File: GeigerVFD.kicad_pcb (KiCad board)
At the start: 2 copper layers, 32 parts, among them IC1 LM555, IC2 TLC555, J3 C-EUC0805, Q1 BD137, T2 2N4401, T3 STN0214, T4 2N4401, U2 ESP32-DEVKITC-32D, U3 MAX6934, U4 FV651G

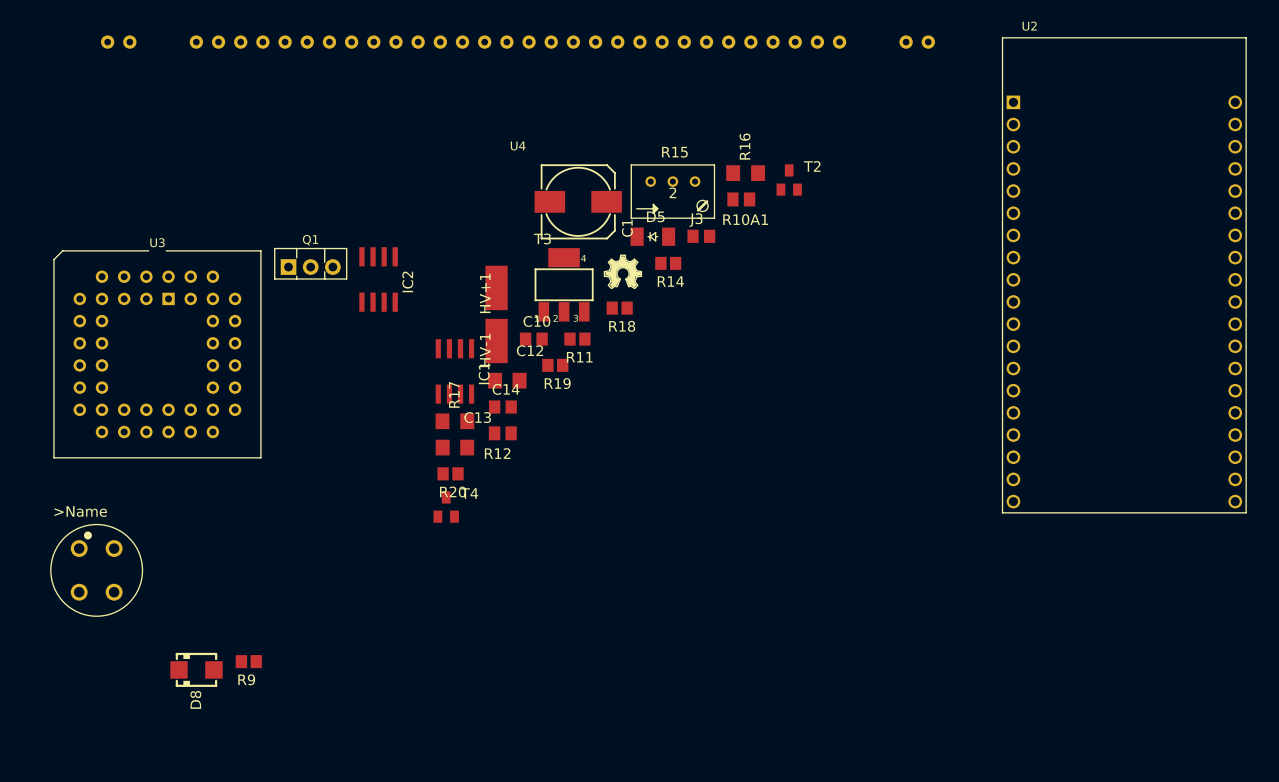
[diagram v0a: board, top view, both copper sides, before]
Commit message: Update footprints & fix bugs
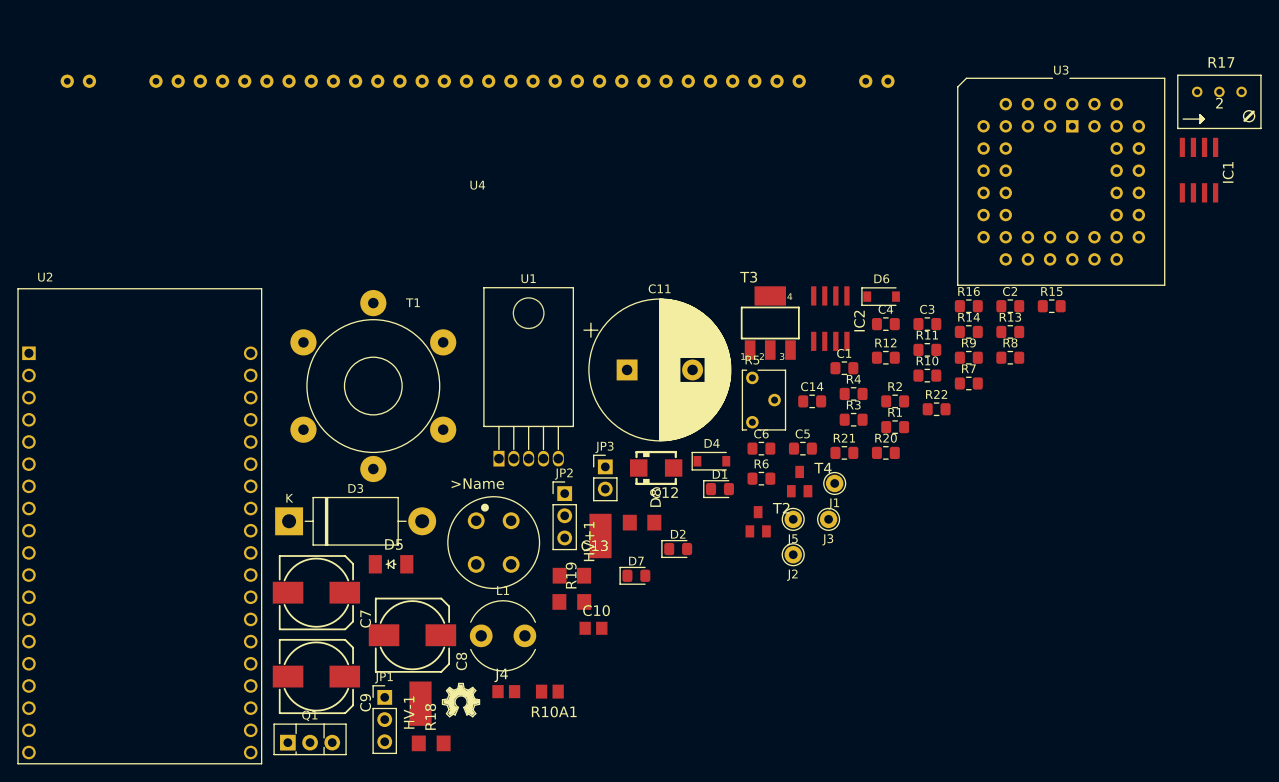
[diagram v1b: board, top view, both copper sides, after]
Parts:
- added C11: 1000µ, Capacitor_THT:CP_Radial_D16.0mm_P7.50mm, F.Cu at (519.9, 205.9)
- added C2: 10n, Capacitor_SMD:C_0805_2012Metric_Pad1.15x1.40mm_HandSolder, F.Cu at (563.8, 198.6)
- added C3: 100n, Capacitor_SMD:C_0805_2012Metric_Pad1.15x1.40mm_HandSolder, F.Cu at (554.3, 200.7)
- added C4: 330n, Capacitor_SMD:C_0805_2012Metric_Pad1.15x1.40mm_HandSolder, F.Cu at (549.6, 200.7)
- added C5: 100n, Capacitor_SMD:C_0805_2012Metric_Pad1.15x1.40mm_HandSolder, F.Cu at (540.1, 214.9)
- added C6: 100n, Capacitor_SMD:C_0805_2012Metric_Pad1.15x1.40mm_HandSolder, F.Cu at (535.3, 214.9)
- added C7: 10uF, PiGI-V1.1:153CLV-0810, F.Cu at (484.4, 231.4)
- added C8: 10uF, PiGI-V1.1:153CLV-0810, F.Cu at (495.4, 236.3)
- added C9: 220uF, PiGI-V1.1:153CLV-0810, F.Cu at (484.4, 241.0)
- added D1: green, LED_SMD:LED_0805_2012Metric_Pad1.15x1.40mm_HandSolder, F.Cu at (530.6, 219.6)
- added D2: yellow, LED_SMD:LED_0805_2012Metric_Pad1.15x1.40mm_HandSolder, F.Cu at (525.8, 226.4)
- added D3: 1N5822, Diode_THT:D_DO-201AD_P15.24mm_Horizontal, F.Cu at (481.2, 223.3)
- added D4: 1N4148, Diode_SMD:D_SOD-123, F.Cu at (529.6, 216.4)
- added D6: 1N4148, Diode_SMD:D_SOD-123, F.Cu at (549.1, 197.5)
- added D7: red, LED_SMD:LED_0805_2012Metric_Pad1.15x1.40mm_HandSolder, F.Cu at (521.0, 229.5)
- added J1: 5V, Connector_Pin:Pin_D1.0mm_L10.0mm, F.Cu at (543.7, 218.9)
- added J2: 3.3V, Connector_Pin:Pin_D1.0mm_L10.0mm, F.Cu at (539.0, 227.1)
- added J4: C-EUC0805, PiGI-V1.1:C0805, F.Cu at (506.1, 242.8)
- added J5: Pulse, Connector_Pin:Pin_D1.0mm_L10.0mm, F.Cu at (539.0, 223.1)
- added JP1: Jumper3, Connector_PinHeader_2.54mm:PinHeader_1x03_P2.54mm_Vertical, F.Cu at (492.2, 243.4)
- added JP2: Jumper3, Connector_PinHeader_2.54mm:PinHeader_1x03_P2.54mm_Vertical, F.Cu at (512.8, 220.1)
- added JP3: Jumper, Connector_PinHeader_2.54mm:PinHeader_1x02_P2.54mm_Vertical, F.Cu at (517.5, 217.0)
- added L1: 100µ, Inductor_THT:L_Radial_D7.8mm_P5.00mm_Fastron_07HCP, F.Cu at (503.2, 236.4)
- added R1: 1k, Resistor_SMD:R_0805_2012Metric_Pad1.15x1.40mm_HandSolder, F.Cu at (550.6, 212.5)
- added R10: 220k, Resistor_SMD:R_0805_2012Metric_Pad1.15x1.40mm_HandSolder, F.Cu at (554.3, 206.6)
- added R13: 1k, Resistor_SMD:R_0805_2012Metric_Pad1.15x1.40mm_HandSolder, F.Cu at (563.8, 201.6)
- added R2: 1k, Resistor_SMD:R_0805_2012Metric_Pad1.15x1.40mm_HandSolder, F.Cu at (550.6, 209.5)
- added R21: 100k, Resistor_SMD:R_0805_2012Metric_Pad1.15x1.40mm_HandSolder, F.Cu at (544.8, 215.4)
- added R22: 27k, Resistor_SMD:R_0805_2012Metric_Pad1.15x1.40mm_HandSolder, F.Cu at (555.4, 210.4)
- added R3: 2.2k, Resistor_SMD:R_0805_2012Metric_Pad1.15x1.40mm_HandSolder, F.Cu at (545.9, 211.6)
- added R4: 1k, Resistor_SMD:R_0805_2012Metric_Pad1.15x1.40mm_HandSolder, F.Cu at (545.9, 208.7)
- added R5: 100k, Potentiometer_THT:Potentiometer_Vishay_T73XX_Horizontal, F.Cu at (534.3, 206.8)
- added R6: 1k, Resistor_SMD:R_0805_2012Metric_Pad1.15x1.40mm_HandSolder, F.Cu at (535.3, 218.4)
- added R7: 2.2k, Resistor_SMD:R_0805_2012Metric_Pad1.15x1.40mm_HandSolder, F.Cu at (559.1, 207.5)
- added R8: 1k, Resistor_SMD:R_0805_2012Metric_Pad1.15x1.40mm_HandSolder, F.Cu at (563.8, 204.5)
- added T1: Transformer_1P_SS, Transformer_THT:Transformer_Toroid_Tapped_Horizontal_D14.0mm_Amidon-T50, F.Cu at (482.9, 212.8)
- added U1: LM2577, Package_TO_SOT_THT:TO-220-5_Horizontal_TabDown, F.Cu at (505.3, 216.1)
- C1: value 220uF -> 4.7n; footprint PiGI-V1.1:153CLV-0810 -> Capacitor_SMD:C_0805_2012Metric_Pad1.15x1.40mm_HandSolder
- C14: footprint PiGI-V1.1:C0805 -> Capacitor_SMD:C_0805_2012Metric_Pad1.15x1.40mm_HandSolder
- J3: value C-EUC0805 -> GND; footprint PiGI-V1.1:C0805 -> Connector_Pin:Pin_D1.0mm_L10.0mm
- R11: value 330 -> 680; footprint PiGI-V1.1:R0805 -> Resistor_SMD:R_0805_2012Metric_Pad1.15x1.40mm_HandSolder
- R12: value 1k -> 330; footprint PiGI-V1.1:M0805 -> Resistor_SMD:R_0805_2012Metric_Pad1.15x1.40mm_HandSolder
- R14: value 100k -> 680; footprint PiGI-V1.1:R0805 -> Resistor_SMD:R_0805_2012Metric_Pad1.15x1.40mm_HandSolder
- R15: value 100 -> 1k; footprint PiGI-V1.1:RJ9W -> Resistor_SMD:R_0805_2012Metric_Pad1.15x1.40mm_HandSolder
- R16: value 1M -> 100k; footprint PiGI-V1.1:R1206 -> Resistor_SMD:R_0805_2012Metric_Pad1.15x1.40mm_HandSolder
- R17: value 4.7M -> 100; footprint PiGI-V1.1:R1206 -> PiGI-V1.1:RJ9W
- R18: value 1.5k -> 1M; footprint PiGI-V1.1:R0805 -> PiGI-V1.1:R1206
- R19: value 100k -> 4.7M; footprint PiGI-V1.1:R0805 -> PiGI-V1.1:R1206
- R20: value 27k -> 1.5k; footprint PiGI-V1.1:R0805 -> Resistor_SMD:R_0805_2012Metric_Pad1.15x1.40mm_HandSolder
- R9: value 220k -> 1k; footprint PiGI-V1.1:R0805 -> Resistor_SMD:R_0805_2012Metric_Pad1.15x1.40mm_HandSolder
- moved U2 116.3 mm to (464.1, 223.8)
- moved U3 105.4 mm to (570.9, 178.0)
- moved R17 94.9 mm to (587.8, 175.2)
- moved R9 89.5 mm to (559.1, 204.5)
- moved IC1 88.3 mm to (585.4, 183.1)
- moved R10A1 60.5 mm to (511.1, 242.8)
- moved D8 57.5 mm to (523.3, 217.2)
- moved Q1 54.5 mm to (481.1, 248.6)
- moved R18 54.3 mm to (497.5, 248.7)
- moved LOGO1 52.4 mm to (498.8, 245.7)
- moved IC2 51.9 mm to (543.2, 200.1)
- moved R20 49.9 mm to (549.6, 215.4)
- moved D5 48.0 mm to (492.9, 228.2)
- moved L2 45.6 mm to (504.7, 225.7)
- moved R15 45.3 mm to (568.6, 198.6)
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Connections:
- IC1 pad 2: Net-(C2-Pad1) (its old number) -> Net-(C1-Pad1)
- IC1 pad 6: Net-(C2-Pad1) (its old number) -> Net-(C1-Pad1)
- IC2 pad 5: Net-(IC2-Pad5) -> (no net)
- J3 pad 1: Net-(J3-Pad1) -> GND
- R11 pad 1: Net-(D5-PadA) -> Net-(R11-Pad1)
- R11 pad 2: Net-(IC2-Pad3) -> Net-(JP1-Pad3)
- R12 pad 1: Net-(IC2-Pad3) -> Net-(D5-PadA)
- R12 pad 2: Net-(IC2-Pad7) -> Net-(IC2-Pad3)
- R14 pad 1: +5V -> Net-(R14-Pad1)
- R14 pad 2: R -> Net-(JP2-Pad3)
- R16 pad 1: Net-(C12-Pad1) -> +5V
- R16 pad 2: Net-(C13-Pad1) -> R
- R18 pad 1: Net-(R18-Pad1) -> Net-(C12-Pad1)
- R18 pad 2: Net-(C14-Pad1) -> Net-(C13-Pad1)
- R19 pad 1: GND -> Net-(C13-Pad1)
- R19 pad 2: Net-(R18-Pad1) -> Net-(HV+1-Pad1)
- R20 pad 1: +3V3 -> Net-(R20-Pad1)
- R20 pad 2: Net-(J3-Pad2) -> Net-(C14-Pad1)
- R9 pad 1: GND -> Net-(D4-Pad2)
- R9 pad 2: Net-(C10-Pad2) -> +5V
- T4 pad 1: Net-(R18-Pad1) -> Net-(R20-Pad1)
- T4 pad 3: Net-(J3-Pad2) -> Net-(J4-Pad2)
- U2 pad 10: Net-(JP2-Pad3) -> Net-(R14-Pad1)
- U2 pad 11: Net-(JP1-Pad3) -> Net-(R11-Pad1)
- U2 pad 12: Net-(U2-Pad12) -> (no net)
- U2 pad 15: Net-(U2-Pad15) -> (no net)
- U2 pad 16: Net-(U2-Pad16) -> (no net)
- U2 pad 17: Net-(U2-Pad17) -> (no net)
- U2 pad 18: Net-(U2-Pad18) -> (no net)
- U2 pad 19: +5V -> Net-(JP3-Pad2)
- U2 pad 2: Net-(U2-Pad2) -> (no net)
- U2 pad 21: Net-(U2-Pad21) -> (no net)
- U2 pad 22: Net-(U2-Pad22) -> (no net)
- U2 pad 23: Net-(U2-Pad23) -> (no net)
- U2 pad 24: Net-(U2-Pad24) -> (no net)
- U2 pad 25: Net-(U2-Pad25) -> (no net)
- U2 pad 29: Net-(U2-Pad29) -> (no net)
- U2 pad 3: Net-(U2-Pad3) -> (no net)
- U2 pad 32: Net-(U2-Pad32) -> (no net)
- U2 pad 33: Net-(U2-Pad33) -> (no net)
- U2 pad 34: Net-(U2-Pad34) -> (no net)
- U2 pad 35: Net-(U2-Pad35) -> (no net)
- U2 pad 36: Net-(U2-Pad36) -> (no net)
- U2 pad 37: Net-(U2-Pad37) -> (no net)
- U2 pad 38: Net-(U2-Pad38) -> (no net)
- U2 pad 4: Net-(U2-Pad4) -> (no net)
- U2 pad 5: Net-(U2-Pad5) -> (no net)
- U2 pad 6: Net-(U2-Pad6) -> (no net)
- U2 pad 7: Net-(J3-Pad1) -> Net-(J4-Pad1)
- U2 pad 8: Net-(U2-Pad8) -> (no net)
- U2 pad 9: Net-(U2-Pad9) -> (no net)
- U3 pad 2: Net-(U3-Pad2) -> (no net)
- U3 pad 26: Net-(U3-Pad26) -> (no net)
- U3 pad 27: Net-(U3-Pad27) -> (no net)
- U3 pad 28: Net-(U3-Pad28) -> (no net)
- U3 pad 29: Net-(U3-Pad29) -> (no net)
- U3 pad 41: Net-(U3-Pad41) -> (no net)
- U3 pad 42: Net-(U3-Pad42) -> (no net)
- U3 pad 6: Net-(U3-Pad6) -> (no net)
- U4 pad 22: Net-(U4-Pad22) -> (no net)
- U4 pad 23: Net-(U4-Pad23) -> (no net)

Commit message: First sort of PCB
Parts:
- moved R7 526.1 mm to (42.2, 109.9)
- moved R3 523.5 mm to (35.3, 95.9)
- moved R15 522.6 mm to (47.0, 166.4)
- moved U3 518.8 mm to (64.1, 67.3), turned to 90 degrees
- moved C4 518.4 mm to (41.9, 95.9)
- moved C3 515.8 mm to (49.3, 95.9), turned to 180 degrees
- moved R11 514.2 mm to (42.3, 156.2), turned to 180 degrees
- moved R14 513.7 mm to (47.6, 153.7), turned to 180 degrees
- moved R6 509.9 mm to (37.1, 109.9)
- moved C11 509.3 mm to (17.9, 120.0)
- moved R5 504.2 mm to (37.5, 120.7), turned to 90 degrees
- moved U1 482.6 mm to (39.4, 90.2)
- moved D7 479.0 mm to (47.0, 160.7)
- moved D3 478.8 mm to (17.8, 102.9)
- moved L1 470.5 mm to (52.1, 102.9), turned to 180 degrees
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
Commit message: Add GM-Tube. First pass at PCB
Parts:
- removed HV+1: HV+, PiGI-V1.1:SMD2,54-5,08
- removed HV-1: HV-, PiGI-V1.1:SMD2,54-5,08
- removed J4: C-EUC0805, PiGI-V1.1:C0805
- added C15: 100n, Capacitor_SMD:C_0805_2012Metric_Pad1.15x1.40mm_HandSolder, F.Cu at (41.9, 49.3)
- added V1: GM-Tube, GeigerVFD:Tube, F.Cu at (116.8, 92.7)
- U4: moved to B.Cu
- moved J1 242.9 mm to (15.2, 109.2), turned to 90 degrees
- moved J3 239.3 mm to (15.2, 104.1), turned to 90 degrees
- moved C5 230.5 mm to (23.1, 114.3), turned to 0 degrees
- moved D1 230.1 mm to (17.8, 109.0), turned to 270 degrees
- moved R1 222.7 mm to (17.8, 103.9), turned to 90 degrees
- moved C7 220.8 mm to (25.4, 106.1), turned to 270 degrees
- moved C9 214.0 mm to (35.6, 106.1), turned to 270 degrees
- moved D2 194.2 mm to (50.8, 114.5), turned to 270 degrees
- moved R2 188.3 mm to (50.8, 110.5), turned to 90 degrees
- moved C6 184.1 mm to (54.6, 111.5), turned to 90 degrees
- moved C8 179.7 mm to (61.0, 111.0), turned to 270 degrees
- moved J2 165.9 mm to (88.9, 120.7), turned to 90 degrees
- moved J5 153.6 mm to (88.9, 124.5), turned to 90 degrees
- moved R22 148.9 mm to (73.2, 124.0)
- moved T4 146.1 mm to (73.3, 129.4), turned to 0 degrees
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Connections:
- net Net-(C14-Pad1) renamed HV-
- J5 pad 1: Net-(J4-Pad1) -> Net-(J5-Pad1)
- R19 pad 2: Net-(HV+1-Pad1) -> HV+
- R22 pad 2: Net-(J4-Pad2) -> Net-(J5-Pad1)
- T4 pad 3: Net-(J4-Pad2) -> Net-(J5-Pad1)
- U2 pad 7: Net-(J4-Pad1) -> Net-(J5-Pad1)
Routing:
- net GND: track 0.00 -> 143.6 mm
- net Vdd: track 0.00 -> 80.3 mm
- net Fil1: track 0.00 -> 75.2 mm
- net Fil2: track 0.00 -> 52.4 mm
- net HV-: track 0.00 -> 51.4 mm
- net +5V: track 0.00 -> 49.0 mm
- net Net-(U2-Pad27): track 0.00 -> 46.5 mm
- net Net-(R10A1-Pad2): track 0.00 -> 40.9 mm
- net Net-(D3-Pad2): track 0.00 -> 39.0 mm
- net Net-(IC2-Pad7): track 0.00 -> 34.2 mm
- net Net-(U2-Pad28): track 0.00 -> 33.7 mm
- net +3V3: track 0.00 -> 31.3 mm
- net Net-(JP2-Pad2): track 0.00 -> 29.8 mm
- net Net-(U2-Pad31): track 0.00 -> 29.6 mm
- net R: track 0.00 -> 28.6 mm
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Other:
- board outline added: 114.3 x 137.2 mm
- net class Power added: clearance 0.2, trace_width 0.5, via_dia 0.8, via_drill 0.4

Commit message: Fix annotations of PiGi subsection. Fix some footprint issues. More PCB routing Add Geiger Tube
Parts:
- removed the C6 at (54.6, 111.5)
- removed the L2 at (88.9, 87.1)
- removed R10A1: 30R, PiGI-V1.1:M0805
- added C10: 100n, Capacitor_SMD:C_0805_2012Metric_Pad1.15x1.40mm_HandSolder, F.Cu at (97.3, 278.6)
- added L1: 15mH, PiGI-V1.1:1200LRS, F.Cu at (72.9, 244.4)
- added R10a1: 30R, PiGI-V1.1:M0805, F.Cu at (64.2, 249.4)
- moved U1 258.1 mm to (45.6, 316.3), turned to 90 degrees
- moved R16 253.1 mm to (50.5, 315.7), turned to 90 degrees
- moved R13 249.9 mm to (54.4, 315.7), turned to 90 degrees
- moved R17 247.4 mm to (50.5, 310.6), turned to 90 degrees
- moved U4 244.5 mm to (12.4, 264.7), turned to 270 degrees
- moved C8 244.1 mm to (54.4, 310.6), turned to 90 degrees
- moved C15 242.1 mm to (35.1, 291.3), turned to 180 degrees
- moved C7 240.9 mm to (52.8, 306.6), turned to 0 degrees
- moved U3 230.7 mm to (31.5, 274.8), turned to 90 degrees
- moved C14 229.9 mm to (73.4, 311.7), turned to 0 degrees
- moved R15 228.7 mm to (55.6, 297.7), turned to 270 degrees
- moved J3 226.5 mm to (89.9, 318.0), turned to 180 degrees
- moved D5 225.9 mm to (62.0, 300.2), turned to 270 degrees
- moved J1 223.5 mm to (95.0, 318.0), turned to 180 degrees
- moved R11 223.5 mm to (89.7, 315.5), turned to 180 degrees
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- renumbered C9 to C1, C7 to C11, C8 to C12, C1 to C13, C11 to C14, C12 to C2, C13 to C3, C10 to C4, C14 to C5, C2 to C6, C3 to C7, C4 to C8, C5 to C9, D8 to D1, D5 to D2, D1 to D3, D2 to D4, D3 to D5, D4 to D6, D6 to D7, D7 to D8, IC2 to IC1, IC1 to IC2, J5 to J4, L1 to L2, R13 to R1, R17 to R10, R1 to R11, R2 to R12, R3 to R13, R4 to R14, R5 to R15, R6 to R16, R7 to R17, R8 to R18, R9 to R19, R18 to R2, R11 to R20, R14 to R21, R15 to R22, R19 to R3, R16 to R4, R12 to R5, R10 to R6, R20 to R7, R21 to R8, R22 to R9, T3 to T1, T4 to T3, T1 to T4
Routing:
- net +5V: track 49.0 -> 86.8 mm, vias 0 -> 2
- net Net-(U2-Pad30): track 26.0 -> 37.9 mm
- net Net-(U2-Pad31): track 29.6 -> 39.0 mm
- net Net-(U2-Pad28): track 33.7 -> 41.7 mm
- net Vdd: track 80.3 -> 87.9 mm
- net HV+: track 21.2 -> 28.0 mm
- net GND: track 143.6 -> 150.1 mm
- net HV-: track 51.4 -> 57.7 mm
- net Net-(U2-Pad27): track 46.5 -> 51.6 mm
- net (no net): track 1.40 -> 0.00 mm
- net Net-(JP2-Pad2): track 29.8 -> 30.4 mm
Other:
- board size 114.3 x 137.2 mm -> 137.2 x 114.3 mm

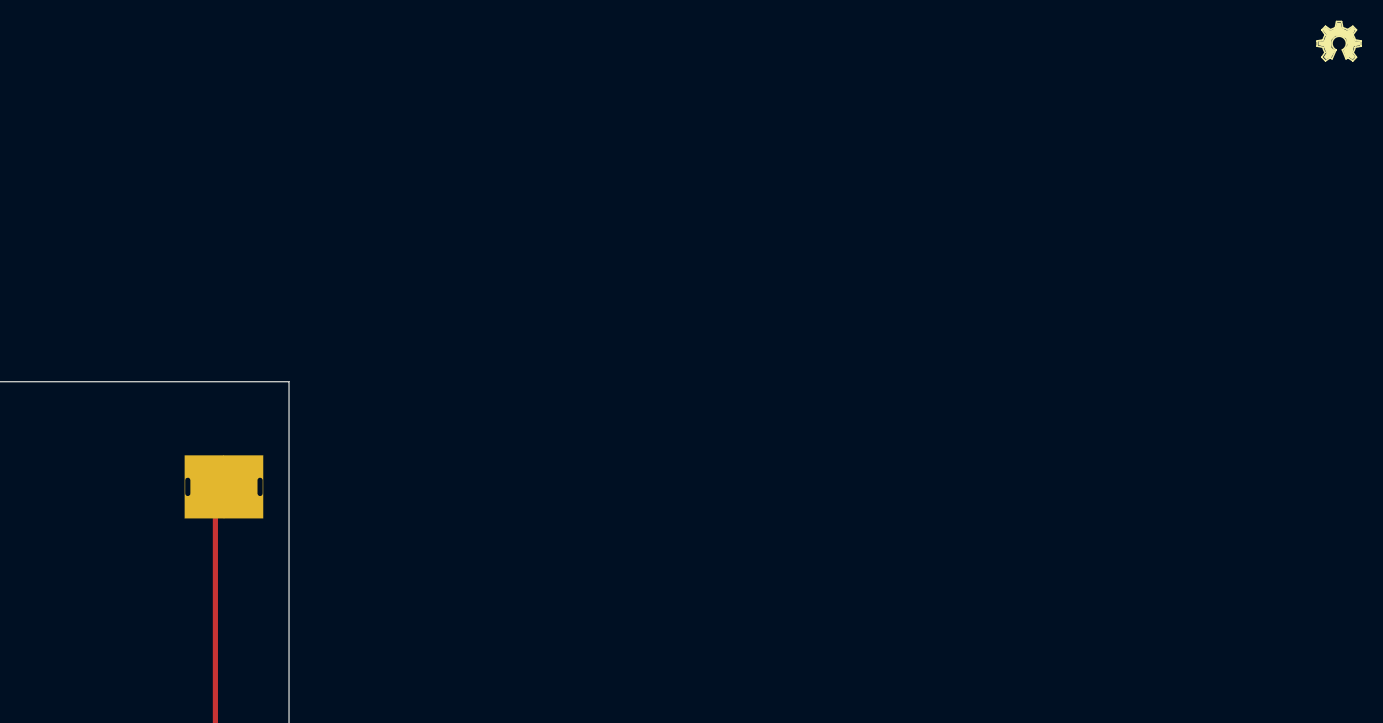
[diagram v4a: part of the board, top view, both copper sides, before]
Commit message: Fix GM Tube Footprint Add Power flags for ERC Fix VFD symbol to use pin stacking
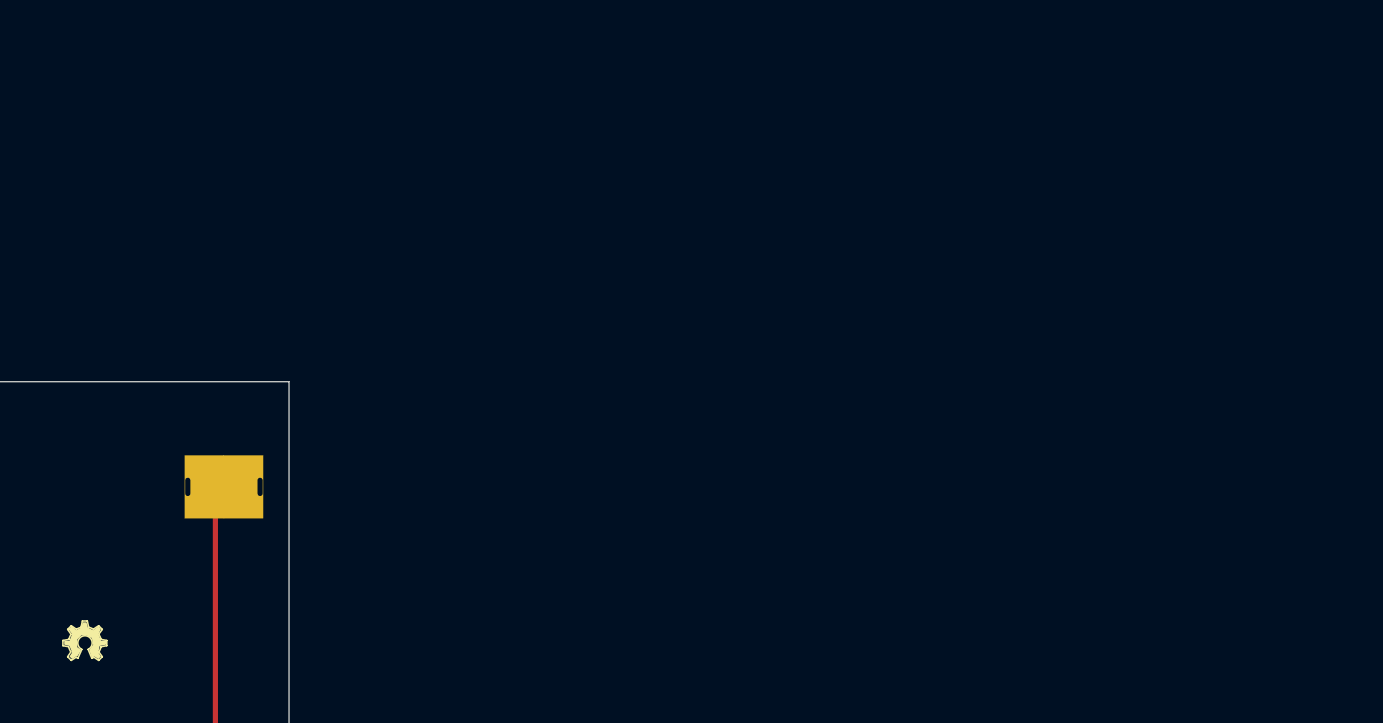
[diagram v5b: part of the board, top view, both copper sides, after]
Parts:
- moved LOGO1 134.3 mm to (113.8, 233.2)
